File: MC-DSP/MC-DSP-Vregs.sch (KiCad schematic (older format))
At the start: 18 parts, among them U20 R-78E3.3-1.0, U21 R-78B1.2-2.0

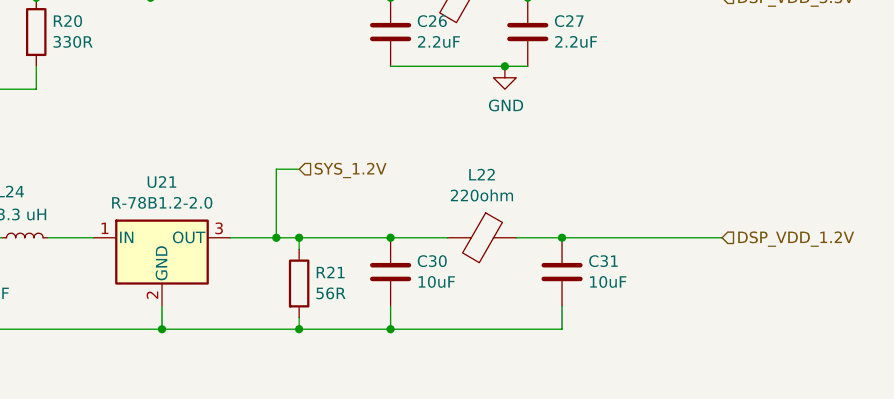
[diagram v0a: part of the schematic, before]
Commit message: DSP breakout to backplane done, just need to route final 11 signals.
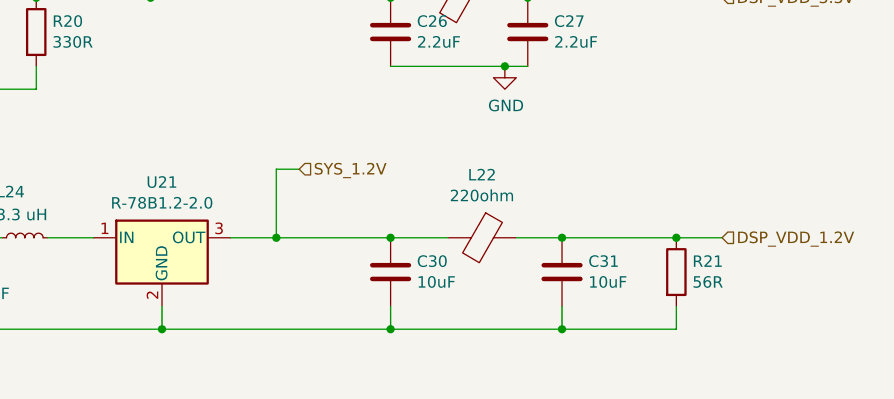
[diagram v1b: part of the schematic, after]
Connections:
- net DSP_VDD_1.2V: now also R21.1
- net SYS_1.2V: no longer R21.1
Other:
- moved on the sheet: R21
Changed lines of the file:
@@
 L Device:R R?
 U 1 1 6245D2FE
-P 7750 4600
+P 9400 4550
 AR Path="/6245D2FE" Ref="R?"  Part="1"
 AR Path="/6187F723/6245D2FE" Ref="R21"  Part="1"
-F 0 "R21" H 7820 4646 50  0000 L CNN
-F 1 "56R" H 7820 4555 50  0000 L CNN
-F 2 "Resistor_SMD:R_0603_1608Metric_Pad0.98x0.95mm_HandSolder" V 7680 4600 50  0001 C CNN
-F 3 "https://www.digikey.com/en/products/detail/yageo/RC0603FR-0756RL/727301?s=N4IgTCBcDaIEoGEAMA2JBmAYnAtEg7AKwpwAyIAugL5A" H 7750 4600 50  0001 C CNN
-	1    7750 4600
+F 0 "R21" H 9470 4596 50  0000 L CNN
+F 1 "56R" H 9470 4505 50  0000 L CNN
+F 2 "Resistor_SMD:R_0603_1608Metric_Pad0.98x0.95mm_HandSolder" V 9330 4550 50  0001 C CNN
+F 3 "https://www.digikey.com/en/products/detail/yageo/RC0603FR-0756RL/727301?s=N4IgTCBcDaIEoGEAMA2JBmAYnAtEg7AKwpwAyIAugL5A" H 9400 4550 50  0001 C CNN
+	1    9400 4550
 	1    0    0    -1
 $EndComp
@@
 Wire Wire Line
 	8150 4700 8150 4800
-Wire Wire Line
-	7750 4450 7750 4400
-Wire Wire Line
-	7750 4400 8150 4400
-Wire Wire Line
-	7750 4750 7750 4800
-Wire Wire Line
-	7750 4800 8150 4800
 Connection ~ 8150 4800
 Wire Wire Line
@@
 Connection ~ 8900 4400
 Wire Wire Line
-	8900 4400 9600 4400
+	8900 4400 9400 4400
 Text HLabel 5900 4400 0    50   Input ~ 0
 SYS_24V
@@
 Wire Wire Line
 	5900 4800 6200 4800
-Connection ~ 7750 4800
-Wire Wire Line
-	7750 4400 7650 4400
-Connection ~ 7750 4400
 Wire Wire Line
 	7150 4700 7150 4800
 Connection ~ 7150 4800
-Wire Wire Line
-	7150 4800 7750 4800
 Wire Wire Line
 	6200 4700 6200 4800
@@
 Wire Wire Line
 	8650 3650 8750 3650
+Connection ~ 9400 4400
+Wire Wire Line
+	9400 4400 9600 4400
+Wire Wire Line
+	9400 4700 9400 4800
+Wire Wire Line
+	9400 4800 8900 4800
+Connection ~ 8900 4800
+Wire Wire Line
+	7650 4400 8150 4400
+Wire Wire Line
+	7150 4800 8150 4800
 $EndSCHEMATC
